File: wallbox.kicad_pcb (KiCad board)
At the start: 2 copper layers, 166.4 x 94.6 mm, 52 parts, among them J1 From Transformer, J2 To Wallbox, J3 UART, J4 Program, Q1 BC547, Q2 BC547, Q3 BC547, SW1 SW_Push, U1 KA78R33, U2 LM7805CT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

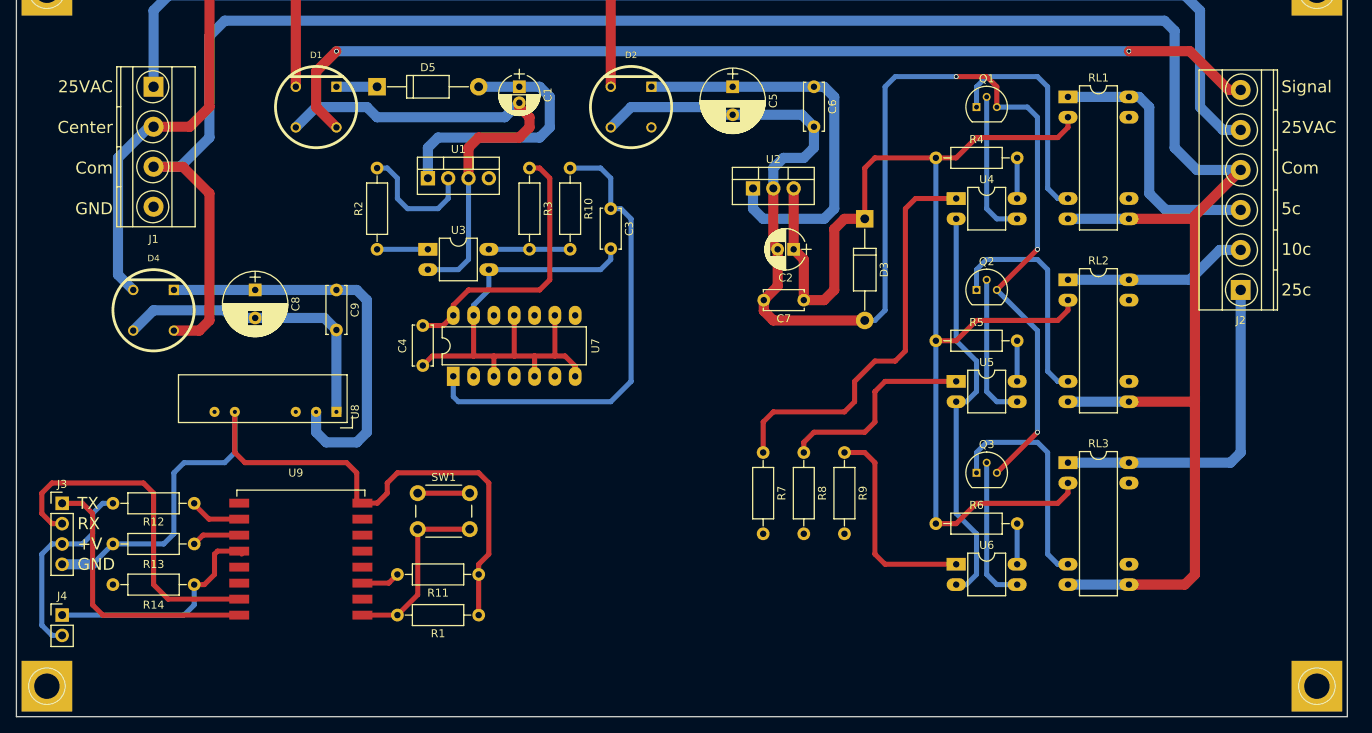
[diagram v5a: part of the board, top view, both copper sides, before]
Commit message: Updated board labels
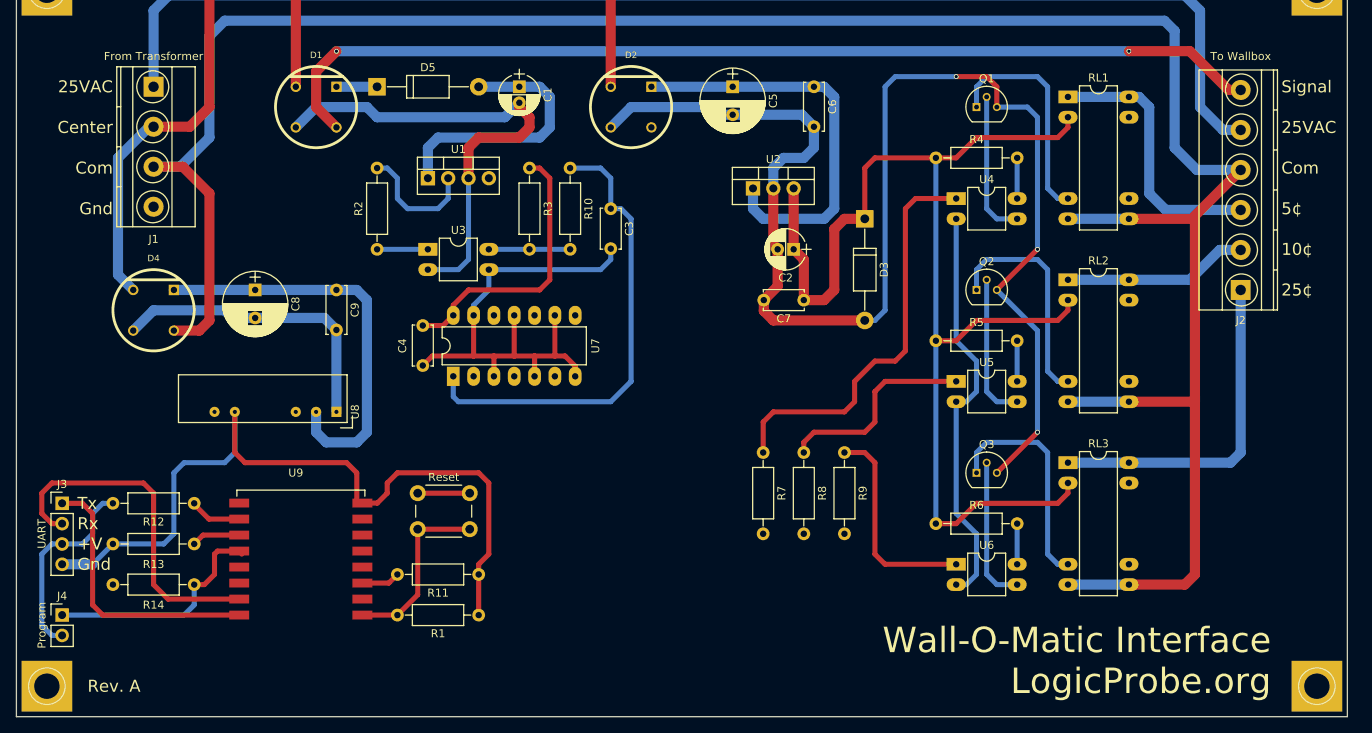
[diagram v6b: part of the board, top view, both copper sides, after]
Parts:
- renumbered SW1 to Reset
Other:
- board text added: "10¢"
- board text added: "25¢"
- board text added: "5¢"
- board text added: "Gnd"
- board text added: "Rev. A"
- board text added: "Rx"
- board text added: "Tx"
- board text added: "Wall-O-Matic Interface LogicProbe.org"
- board text removed: "10c"
- board text removed: "25c"
- board text removed: "5c"
- board text removed: "GND"
- board text removed: "RX"
- board text removed: "TX"
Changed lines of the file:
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@@
     (area 12.014999 12.014999 178.485001 106.730001)
     (thickness 1.6)
-    (drawings 18)
+    (drawings 20)
     (tracks 368)
     (zones 0)
@@
   )
   (setup
-    (last_trace_width 1.27)
+    (last_trace_width 0.25)
     (user_trace_width 0.254)
     (user_trace_width 0.635)
@@
       (effects (font (size 1 1) (thickness 0.15)))
     )
-    (fp_text value "From Transformer" (at -3.81 0 360) (layer F.Fab)
+    (fp_text value "From Transformer" (at -3.81 0 360) (layer F.SilkS)
       (effects (font (size 1 1) (thickness 0.15)))
     )
@@
       (effects (font (size 1 1) (thickness 0.15)))
     )
-    (fp_text value "To Wallbox" (at 29.21 0 180) (layer F.Fab)
+    (fp_text value "To Wallbox" (at 29.21 0 180) (layer F.SilkS)
       (effects (font (size 1 1) (thickness 0.15)))
     )
@@
       (effects (font (size 1 1) (thickness 0.15)))
     )
-    (fp_text value UART (at -2.54 3.81 90) (layer F.Fab)
+    (fp_text value UART (at -2.54 3.81 90) (layer F.SilkS)
       (effects (font (size 1 1) (thickness 0.15)))
     )
@@
       (effects (font (size 1 1) (thickness 0.15)))
     )
-    (fp_text value Program (at -2.54 1.27 90) (layer F.Fab)
+    (fp_text value Program (at -2.54 1.27 90) (layer F.SilkS)
       (effects (font (size 1 1) (thickness 0.15)))
     )
@@
     (descr "tactile push button, 6x6mm e.g. PHAP33xx series, height=5mm")
     (tags "tact sw push 6mm")
-    (fp_text reference SW1 (at 3.25 -2) (layer F.SilkS)
+    (fp_text reference Reset (at 3.25 -2) (layer F.SilkS)
       (effects (font (size 1 1) (thickness 0.15)))
     )
@@
     (pad "" thru_hole rect (at 0 0) (size 6.35 6.35) (drill 3.175) (layers *.Cu *.Mask))
   )
+  (gr_text "Rev. A" (at 20.955 102.87) (layer F.SilkS)
+    (effects (font (size 1.5 1.5) (thickness 0.3)) (justify left))
+  )
+  (gr_text "Wall-O-Matic Interface\nLogicProbe.org" (at 168.91 99.695) (layer F.SilkS)
+    (effects (font (size 3.175 3.175) (thickness 0.508)) (justify right))
+  )
   (gr_line (start 12.065 106.68) (end 12.065 12.065) (angle 90) (layer Edge.Cuts) (width 0.1))
   (gr_line (start 178.435 106.68) (end 12.065 106.68) (angle 90) (layer Edge.Cuts) (width 0.1))
   (gr_line (start 178.435 12.065) (end 178.435 106.68) (angle 90) (layer Edge.Cuts) (width 0.1))
   (gr_line (start 12.065 12.065) (end 178.435 12.065) (angle 90) (layer Edge.Cuts) (width 0.1))
-  (gr_text GND (at 19.685 87.63) (layer F.SilkS)
+  (gr_text Gnd (at 19.685 87.63) (layer F.SilkS)
     (effects (font (size 1.5 1.5) (thickness 0.3)) (justify left))
   )
@@
     (effects (font (size 1.5 1.5) (thickness 0.3)) (justify left))
   )
-  (gr_text RX (at 19.685 82.55) (layer F.SilkS)
+  (gr_text Rx (at 19.685 82.55) (layer F.SilkS)
     (effects (font (size 1.5 1.5) (thickness 0.3)) (justify left))
   )
-  (gr_text TX (at 19.685 80.01) (layer F.SilkS)
+  (gr_text Tx (at 19.685 80.01) (layer F.SilkS)
     (effects (font (size 1.5 1.5) (thickness 0.3)) (justify left))
   )
-  (gr_text GND (at 24.13 43.18) (layer F.SilkS)
+  (gr_text Gnd (at 24.13 43.18) (layer F.SilkS)
     (effects (font (size 1.5 1.5) (thickness 0.3)) (justify right))
   )
@@
     (effects (font (size 1.5 1.5) (thickness 0.3)) (justify right))
   )
-  (gr_text 25c (at 170.18 53.34) (layer F.SilkS)
+  (gr_text 25¢ (at 170.18 53.34) (layer F.SilkS)
     (effects (font (size 1.5 1.5) (thickness 0.3)) (justify left))
   )
-  (gr_text 10c (at 170.18 48.26) (layer F.SilkS)
+  (gr_text 10¢ (at 170.18 48.26) (layer F.SilkS)
     (effects (font (size 1.5 1.5) (thickness 0.3)) (justify left))
   )
-  (gr_text 5c (at 170.18 43.18) (layer F.SilkS)
+  (gr_text 5¢ (at 170.18 43.18) (layer F.SilkS)
     (effects (font (size 1.5 1.5) (thickness 0.3)) (justify left))
   )

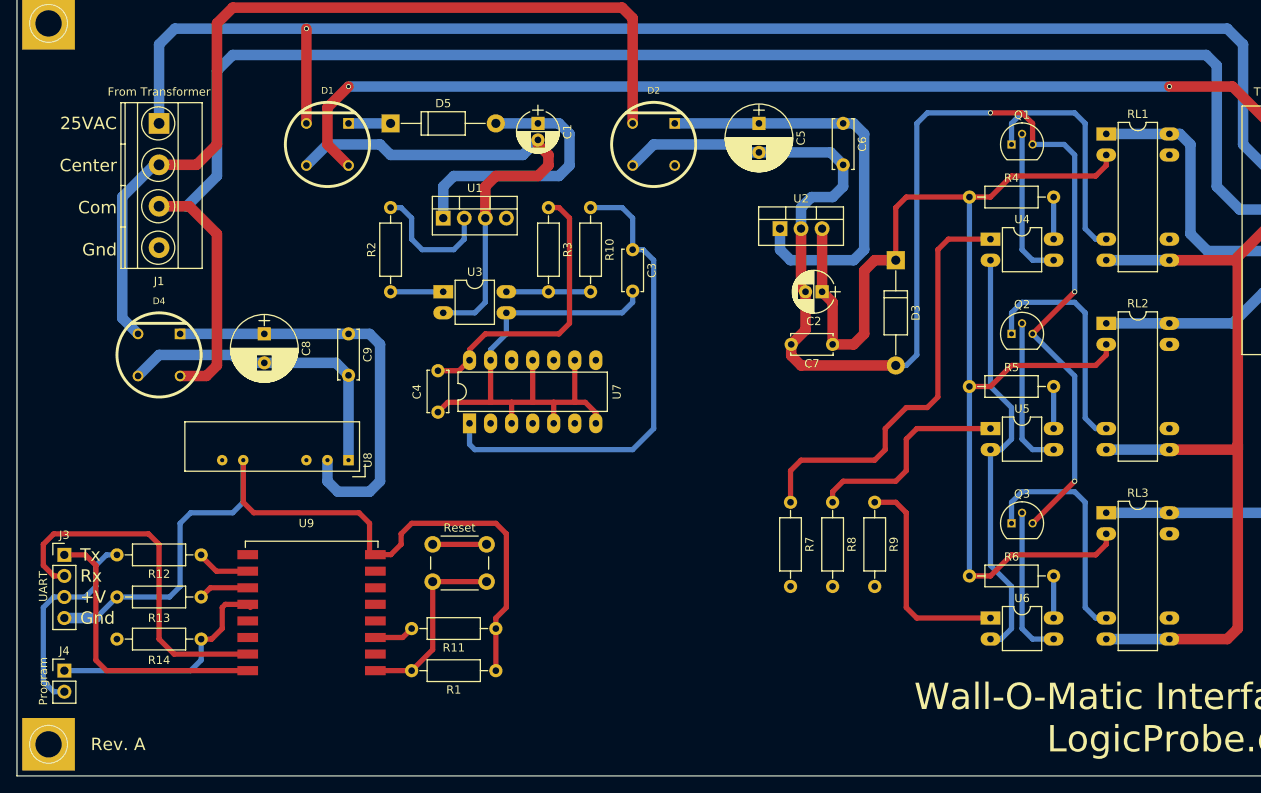
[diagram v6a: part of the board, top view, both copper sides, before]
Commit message: Initial PCB layout complete
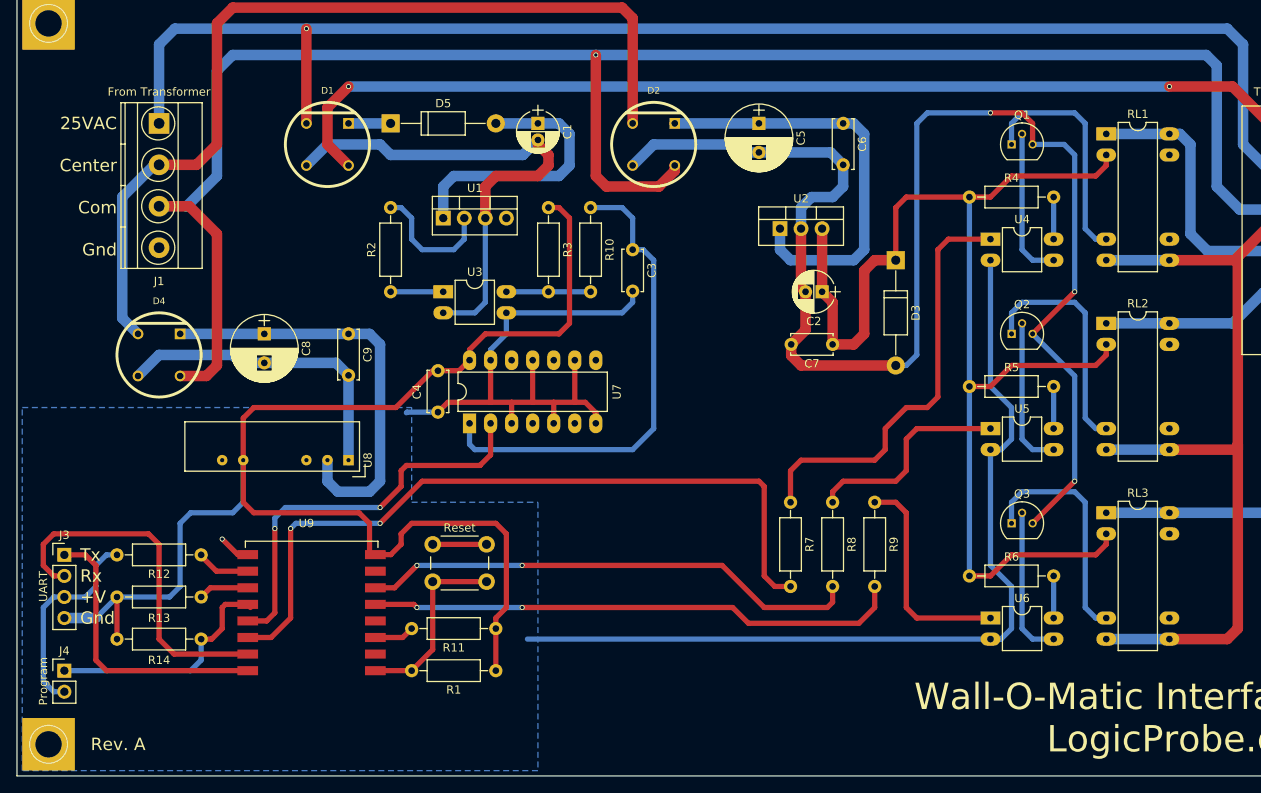
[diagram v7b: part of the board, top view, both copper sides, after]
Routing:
- net Net-(R7-Pad2): track 0.00 -> 90.5 mm, vias 0 -> 2
- net Net-(R9-Pad2): track 0.00 -> 65.2 mm, vias 0 -> 2
- net GND: track 148.2 -> 212.4 mm, vias 0 -> 1
- net Net-(R8-Pad2): track 0.00 -> 61.3 mm, vias 0 -> 2
- net Net-(U7-Pad2): track 0.00 -> 48.5 mm, vias 0 -> 2
- net VCC: track 133.2 -> 169.2 mm
- net Net-(D2-Pad2): track 298.1 -> 324.2 mm, vias 0 -> 1
- added copper zone on B.Cu, net GND
